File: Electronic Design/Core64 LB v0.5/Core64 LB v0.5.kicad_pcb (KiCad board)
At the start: 2 copper layers, 85 x 170 mm, 153 parts, among them IC1 TPS7A0533PDBVR, IC2 LP3961EMP-5.0, J1 HEADER_8-PIN_0.1, J10 TSM-106-03-T-DV‎, J11 SSW-116-22-F-S-VS‎, J12 TEENSY Cur. Mon., J13 Core Cur. Mon., J14 SSW-116-22-F-S-VS‎, J17 LED Cur. Mon., J2 HEADER_11-PIN_0.1, J3 Conn_01x08_Female, J4 PRG, J5 HEADER_8-PIN_0.1, J6 HEADER_8-PIN_0.1, J7 S03B-PASK-2_LF__SN_, J8 5V0 Cur. Mon., J9 3V3 Cur. Mon., Q1 MCC_SL3401A, Q10 MMBT4403LT1G, Q11 MMBT4403LT1G, Q12 MMBT4401LT1G, Q13 MMBT4403LT1G, Q14 MMBT4403LT1G, Q15 MMBT4401LT1G, Q16 MMBT4403LT1G, Q17 MMBT4403LT1G, Q18 MMBT4401LT1G, Q19 MMBT4401LT1G, Q2 MMBT4403LT1G, Q20 MMBT4401LT1G, Q21 MMBT4401LT1G, Q22 Q_NMOS_DGS_NVTR4503NT1G, Q3 MMBT4403LT1G, Q4 MMBT4403LT1G, Q5 MMBT4403LT1G, Q6 MMBT4401LT1G, Q7 MMBT4401LT1G, Q8 MMBT4401LT1G, Q9 MMBT4401LT1G, SW1 JS102011SAQN, U1 74HC02, U2 Teensy3.2, U3 SN74LV1T125DBVR, U4 M24C01-RMN, U5 74HC238, U6 Micro_LiPo_Charger, U7 LM393, U8 Adafruit_3.2_TFT_1743, X1 QWIIC, X2 Header_9-PIN_0.1, X3 SAO_conn_SFH11-NBPC-D03-ST-BK, X4 SSW-104-22-L-S-VS

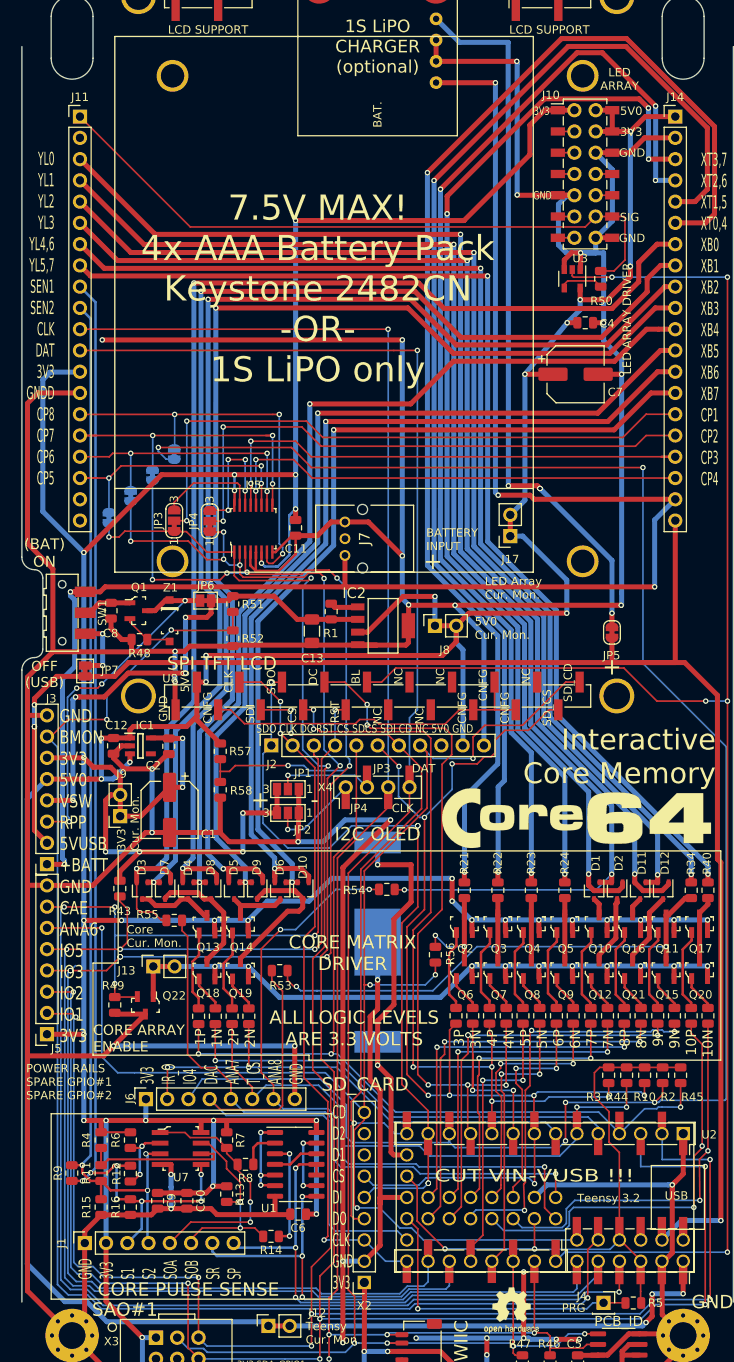
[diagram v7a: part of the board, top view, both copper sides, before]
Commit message: Update schematic battery and LiPo charger notes, move SD_CD from ANA_6 to SPARE_3, schematic red lines
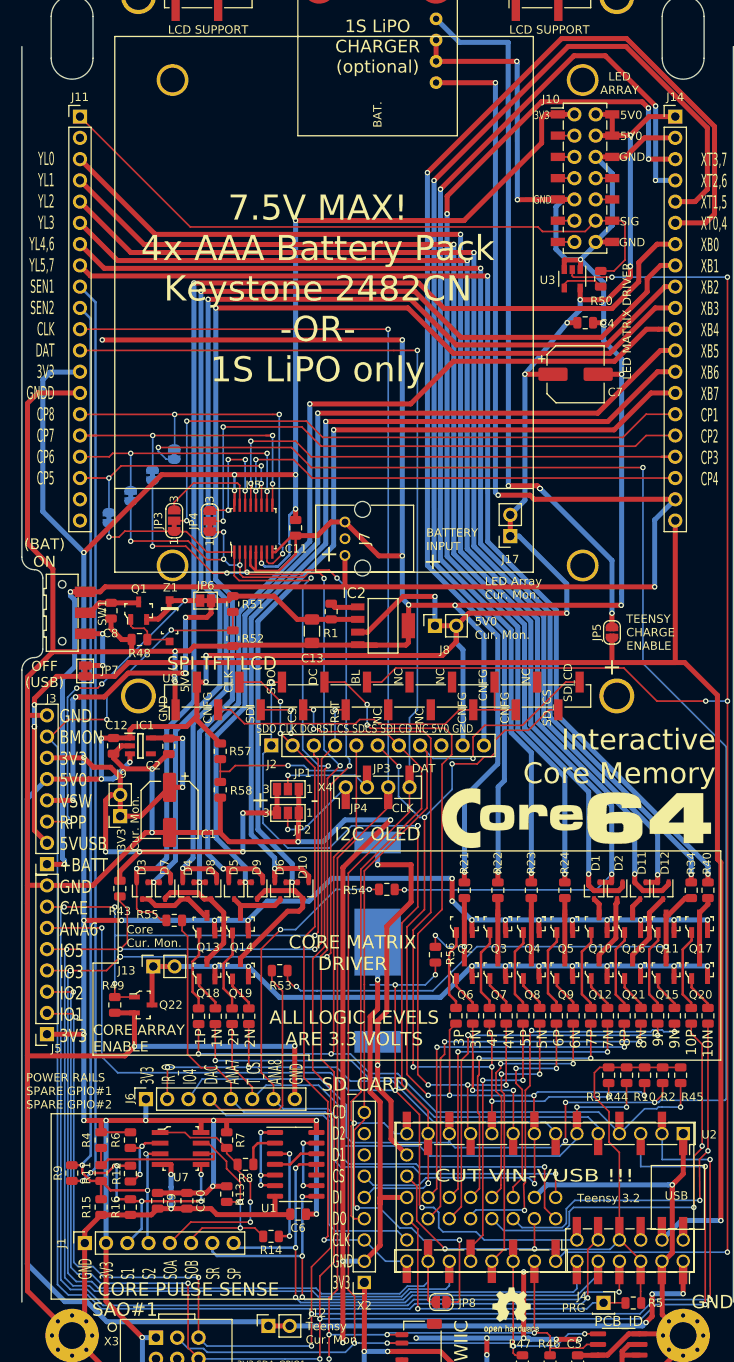
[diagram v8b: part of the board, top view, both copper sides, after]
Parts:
- added JP8: SD CARD DETECT, Jumper:SolderJumper-2_P1.3mm_Open_RoundedPad1.0x1.5mm, F.Cu at (7.60, 117.5)
- J7: footprint JST_S03B-PASK-2_LF__SN_:S03BPASK2LFSN -> JST_S03B-PASK-2_LF__SN_:S03BPASK2LFSN_.075in_holes
- JP5: footprint Jumper:SolderJumper-2_P1.3mm_Bridged_RoundedPad1.0x1.5mm -> Jumper:SolderJumper-2_P1.3mm_Open_RoundedPad1.0x1.5mm
- moved J10 0.50 mm to (0.00, 0.50)
- moved Q22 0.25 mm to (-28.0, 82.0), turned to 0 degrees
- turned Q1 to 90 degrees
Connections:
- net LED_ARRAY_3V3_SIG renamed LED_MATRIX_3V3_SIG
- net LED_ARRAY_5V0_SIG renamed LED_MATRIX_5V0_SIG
- J5 pad 6: SD_SPI_CD -> SPARE_ANA_6
- Q1 pad 1: Net-(C8-Pad1) -> Net-(Q1-Pad1)
- Q1 pad 2: Net-(Q1-Pad2) -> +RPP
- Q1 pad 3: +RPP -> Net-(C8-Pad1)
- Q22 pad 1: GNDPWR -> OLED_SPI_DC
- Q22 pad 2: OLED_SPI_DC -> -BATT
- Q22 pad 3: -BATT -> GNDPWR
- R48 pad 1: Net-(Q1-Pad2) -> Net-(Q1-Pad1)
- R56 pad 1: SD_SPI_CD -> SPARE_ANA_6
- U2 pad 37: SD_SPI_CD -> SPARE_ANA_6
- Z1 pad 2: Net-(Q1-Pad2) -> Net-(Q1-Pad1)
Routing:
- net SPARE_ANA_6: track 0.00 -> 117.5 mm, vias 0 -> 5
- net SD_SPI_CD: track 178.7 -> 107.1 mm, vias 5 -> 3
- net -BATT: track 918.5 -> 911.1 mm
- net Net-(Q1-Pad1): track 0.00 -> 6.74 mm
- net Net-(Q1-Pad2): track 6.12 -> 0.00 mm
- net 5V0_MON: track 223.4 -> 225.2 mm
- net Net-(C8-Pad1): track 5.83 -> 6.92 mm
- net +RPP: track 43.3 -> 44.4 mm
- net GNDPWR: track 87.9 -> 89.0 mm
- net Net-(BT1-Pad1): track 48.1 -> 47.2 mm
- net 3V3: track 577.7 -> 577.1 mm
- net 5V0: track 357.2 -> 356.7 mm
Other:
- board text added: "LED MATRIX DRIVER"
- board text added: "TEENSY CHARGE ENABLE"
- board text removed: "LED ARRAY DRIVER"
